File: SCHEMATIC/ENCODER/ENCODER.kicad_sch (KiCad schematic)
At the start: 13 parts, among them J1 Analog OUT, J2 I2C OUT, SW1 mode sel, U1 magnetic_encoder_AS5600

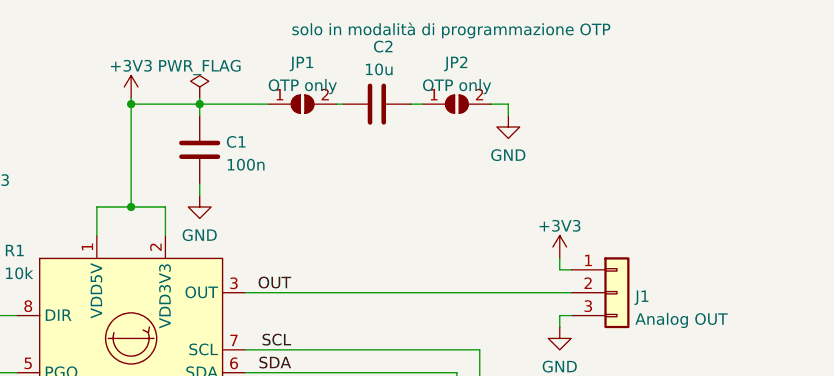
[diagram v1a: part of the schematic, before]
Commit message: iniziato lo broglio. Prima di continuare modificare pin schema
iniziato lo sbroglio della scheda, prima di continuare bisogna sistemare i pin che siano concordi con quelli degli altro (ovvero sistemarli come da tabella su telegram)
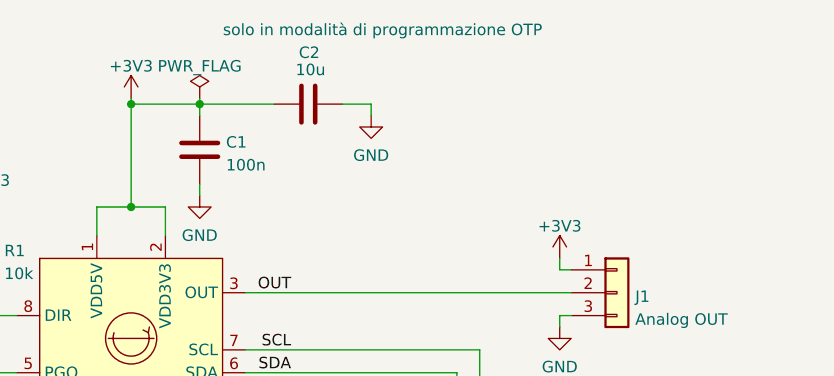
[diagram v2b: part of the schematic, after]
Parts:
- removed JP1, JP2: OTP only, Jumper:SolderJumper-2_P1.3mm_Open_RoundedPad1.0x1.5mm, symbol Jumper:SolderJumper_2_Open
- C2: footprint Capacitor_SMD:C_0603_1608Metric -> Connector_PinSocket_2.54mm:PinSocket_1x02_P2.54mm_Vertical
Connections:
- net +3V3: now also C2.1
- net GND: now also C2.2
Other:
- moved on the sheet: C2
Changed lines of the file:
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@@
     (stroke (width 0) (type default) (color 0 0 0 0))
   )
-  (wire (pts (xy 124.46 76.835) (xy 132.08 76.835))
+  (wire (pts (xy 124.46 76.835) (xy 132.715 76.835))
     (stroke (width 0) (type default) (color 0 0 0 0))
   )
@@
     (stroke (width 0) (type default) (color 0 0 0 0))
   )
-  (wire (pts (xy 139.7 76.835) (xy 140.335 76.835))
-    (stroke (width 0) (type default) (color 0 0 0 0))
-  )
   (wire (pts (xy 164.465 93.98) (xy 164.465 95.25))
     (stroke (width 0) (type default) (color 0 0 0 0))
@@
     (stroke (width 0) (type default) (color 0 0 0 0))
   )
-  (wire (pts (xy 147.955 76.835) (xy 149.225 76.835))
-    (stroke (width 0) (type default) (color 0 0 0 0))
-  )
   (wire (pts (xy 116.84 88.265) (xy 120.65 88.265))
     (stroke (width 0) (type default) (color 0 0 0 0))
   )
-  (wire (pts (xy 156.845 76.835) (xy 158.75 76.835))
+  (wire (pts (xy 140.335 76.835) (xy 143.51 76.835))
     (stroke (width 0) (type default) (color 0 0 0 0))
   )
@@
     (stroke (width 0) (type default) (color 0 0 0 0))
   )
-  (wire (pts (xy 158.75 76.835) (xy 158.75 78.105))
+  (wire (pts (xy 143.51 76.835) (xy 143.51 78.105))
     (stroke (width 0) (type default) (color 0 0 0 0))
   )
@@
     (pin "4")
   )
-  (symbol (lib_id "Jumper:SolderJumper_2_Open") (at 135.89 76.835 0) (unit 1)
-    (in_bom yes) (on_board yes) (fields_autoplaced)
-    (property "Reference" "JP1" (id 0) (at 135.89 72.2462 0))
-    (property "Value" "OTP only" (id 1) (at 135.89 74.7831 0))
-    (property "Footprint" "Jumper:SolderJumper-2_P1.3mm_Open_RoundedPad1.0x1.5mm" (id 2) (at 135.89 76.835 0)
-      (effects (font (size 1.27 1.27)) hide)
-    )
-    (property "Datasheet" "~" (id 3) (at 135.89 76.835 0)
-      (effects (font (size 1.27 1.27)) hide)
-    )
-    (pin "1")
-    (pin "2")
-  )
   (symbol (lib_id "power:GND") (at 164.465 127 0) (unit 1)
     (in_bom yes) (on_board yes) (fields_autoplaced)
@@
     (pin "2")
   )
-  (symbol (lib_id "Device:C") (at 144.145 76.835 90) (unit 1)
+  (symbol (lib_id "Device:C") (at 136.525 76.835 90) (unit 1)
     (in_bom yes) (on_board yes)
-    (property "Reference" "C2" (id 0) (at 146.05 70.4881 90)
-      (effects (font (size 1.27 1.27)) (justify left))
-    )
-    (property "Value" "10u" (id 1) (at 146.05 73.025 90)
-      (effects (font (size 1.27 1.27)) (justify left))
-    )
-    (property "Footprint" "Capacitor_SMD:C_0603_1608Metric" (id 2) (at 147.955 75.8698 0)
-      (effects (font (size 1.27 1.27)) hide)
-    )
-    (property "Datasheet" "~" (id 3) (at 144.145 76.835 0)
-      (effects (font (size 1.27 1.27)) hide)
-    )
-    (property "case" "solo in modalità di programmazione OTP" (id 4) (at 152.4 68.58 90))
+    (property "Reference" "C2" (id 0) (at 137.795 71.12 90)
+      (effects (font (size 1.27 1.27)) (justify left))
+    )
+    (property "Value" "10u" (id 1) (at 138.43 73.025 90)
+      (effects (font (size 1.27 1.27)) (justify left))
+    )
+    (property "Footprint" "Connector_PinSocket_2.54mm:PinSocket_1x02_P2.54mm_Vertical" (id 2) (at 140.335 75.8698 0)
+      (effects (font (size 1.27 1.27)) hide)
+    )
+    (property "Datasheet" "~" (id 3) (at 136.525 76.835 0)
+      (effects (font (size 1.27 1.27)) hide)
+    )
+    (property "case" "solo in modalità di programmazione OTP" (id 4) (at 144.78 68.58 90))
     (pin "1")
     (pin "2")
@@
     (pin "3")
   )
-  (symbol (lib_id "power:GND") (at 158.75 78.105 0) (unit 1)
-    (in_bom yes) (on_board yes) (fields_autoplaced)
-    (property "Reference" "#PWR06" (id 0) (at 158.75 84.455 0)
-      (effects (font (size 1.27 1.27)) hide)
-    )
-    (property "Value" "GND" (id 1) (at 158.75 82.5484 0))
-    (property "Footprint" "" (id 2) (at 158.75 78.105 0)
-      (effects (font (size 1.27 1.27)) hide)
-    )
-    (property "Datasheet" "" (id 3) (at 158.75 78.105 0)
+  (symbol (lib_id "power:GND") (at 143.51 78.105 0) (unit 1)
+    (in_bom yes) (on_board yes) (fields_autoplaced)
+    (property "Reference" "#PWR06" (id 0) (at 143.51 84.455 0)
+      (effects (font (size 1.27 1.27)) hide)
+    )
+    (property "Value" "GND" (id 1) (at 143.51 82.5484 0))
+    (property "Footprint" "" (id 2) (at 143.51 78.105 0)
+      (effects (font (size 1.27 1.27)) hide)
+    )
+    (property "Datasheet" "" (id 3) (at 143.51 78.105 0)
       (effects (font (size 1.27 1.27)) hide)
     )
@@
     )
     (pin "1")
-  )
-  (symbol (lib_id "Jumper:SolderJumper_2_Open") (at 153.035 76.835 0) (unit 1)
-    (in_bom yes) (on_board yes) (fields_autoplaced)
-    (property "Reference" "JP2" (id 0) (at 153.035 72.2462 0))
-    (property "Value" "OTP only" (id 1) (at 153.035 74.7831 0))
-    (property "Footprint" "Jumper:SolderJumper-2_P1.3mm_Open_RoundedPad1.0x1.5mm" (id 2) (at 153.035 76.835 0)
-      (effects (font (size 1.27 1.27)) hide)
-    )
-    (property "Datasheet" "~" (id 3) (at 153.035 76.835 0)
-      (effects (font (size 1.27 1.27)) hide)
-    )
-    (pin "1")
-    (pin "2")
   )
   (symbol (lib_id "Switch:SW_DIP_x02") (at 84.455 104.775 0) (unit 1)
@@
     )
     (path "/75c61f62-7d82-46d3-bb6d-ff97aae5307f"
-      (reference "C2") (unit 1) (value "10u") (footprint "Capacitor_SMD:C_0603_1608Metric")
+      (reference "C2") (unit 1) (value "10u") (footprint "Connector_PinSocket_2.54mm:PinSocket_1x02_P2.54mm_Vertical")
     )
     (path "/0fa8d31e-f571-42a1-ba5e-cfb620e305ea"
@@
       (reference "J2") (unit 1) (value "I2C OUT") (footprint "Connector_JST:JST_XH_B4B-XH-A_1x04_P2.50mm_Vertical")
     )
-    (path "/515574e6-a842-4fe9-a950-2b16c5a079b3"
-      (reference "JP1") (unit 1) (value "OTP only") (footprint "Jumper:SolderJumper-2_P1.3mm_Open_RoundedPad1.0x1.5mm")
-    )
-    (path "/e543ee8a-8fbc-4c18-bbba-c4fbdcb5aed8"
-      (reference "JP2") (unit 1) (value "OTP only") (footprint "Jumper:SolderJumper-2_P1.3mm_Open_RoundedPad1.0x1.5mm")
-    )
     (path "/a6c0f32c-6acc-48b4-b8db-c454596c9e00"
